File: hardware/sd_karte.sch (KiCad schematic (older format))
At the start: 9 parts, among them CON1 SD_Card

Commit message: Weiter am Schaltplan gezeichnet ... noch sehr Fehlerhaft
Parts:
- renumbered R1 to R2, R2 to R3, R3 to R4, R4 to R5, R5 to R6, R6 to R7
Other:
- moved on the sheet: CON1, D1, D2, R2, R3, R4, R5, R6, R7
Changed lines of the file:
@@
 L SD_Card CON1
 U 1 1 55F7A1C8
-P 6500 3800
-F 0 "CON1" H 5850 4350 50  0000 C CNN
-F 1 "SD_Card" H 7100 3250 50  0000 C CNN
-F 2 "10067847-001" H 6700 4150 50  0000 C CNN
-F 3 "" H 6500 3800 60  0000 C CNN
-	1    6500 3800
+P 6700 3700
+F 0 "CON1" H 6050 4250 50  0000 C CNN
+F 1 "SD_Card" H 7300 3150 50  0000 C CNN
+F 2 "10067847-001" H 6900 4050 50  0000 C CNN
+F 3 "" H 6700 3700 60  0000 C CNN
+	1    6700 3700
 	1    0    0    -1
 $EndComp
 $Comp
-L GND #PWR4
+L GND #PWR010
 U 1 1 55F7A326
-P 5500 4250
-F 0 "#PWR4" H 5500 4000 50  0001 C CNN
-F 1 "GND" H 5500 4100 50  0000 C CNN
-F 2 "" H 5500 4250 60  0000 C CNN
-F 3 "" H 5500 4250 60  0000 C CNN
-	1    5500 4250
+P 5700 4150
+F 0 "#PWR010" H 5700 3900 50  0001 C CNN
+F 1 "GND" H 5700 4000 50  0000 C CNN
+F 2 "" H 5700 4150 60  0000 C CNN
+F 3 "" H 5700 4150 60  0000 C CNN
+	1    5700 4150
 	1    0    0    -1
 $EndComp
@@
 L D D1
 U 1 1 55F7A3CC
-P 5250 4400
-F 0 "D1" H 5250 4500 50  0000 C CNN
-F 1 "1N4148" H 5250 4300 50  0000 C CNN
-F 2 "" H 5250 4400 60  0000 C CNN
-F 3 "" H 5250 4400 60  0000 C CNN
-	1    5250 4400
+P 5450 4300
+F 0 "D1" H 5450 4400 50  0000 C CNN
+F 1 "1N4148" H 5450 4200 50  0000 C CNN
+F 2 "" H 5450 4300 60  0000 C CNN
+F 3 "" H 5450 4300 60  0000 C CNN
+	1    5450 4300
 	0    1    1    0
 $EndComp
@@
 L D D2
 U 1 1 55F7A4EB
-P 5250 4800
-F 0 "D2" H 5250 4900 50  0000 C CNN
-F 1 "1N4148" H 5250 4700 50  0000 C CNN
-F 2 "" H 5250 4800 60  0000 C CNN
-F 3 "" H 5250 4800 60  0000 C CNN
-	1    5250 4800
+P 5450 4700
+F 0 "D2" H 5450 4800 50  0000 C CNN
+F 1 "1N4148" H 5450 4600 50  0000 C CNN
+F 2 "" H 5450 4700 60  0000 C CNN
+F 3 "" H 5450 4700 60  0000 C CNN
+	1    5450 4700
 	0    1    1    0
 $EndComp
 $Comp
-L +5V #PWR5
+L +5V #PWR011
 U 1 1 55F7A887
-P 5250 5050
-F 0 "#PWR5" H 5250 4900 50  0001 C CNN
-F 1 "+5V" H 5250 5190 50  0000 C CNN
-F 2 "" H 5250 5050 60  0000 C CNN
-F 3 "" H 5250 5050 60  0000 C CNN
-	1    5250 5050
+P 5450 4950
+F 0 "#PWR011" H 5450 4800 50  0001 C CNN
+F 1 "+5V" H 5450 5090 50  0000 C CNN
+F 2 "" H 5450 4950 60  0000 C CNN
+F 3 "" H 5450 4950 60  0000 C CNN
+	1    5450 4950
 	-1   0    0    1
 $EndComp
-NoConn ~ 5600 4200
-NoConn ~ 7400 3600
-NoConn ~ 7400 3700
-NoConn ~ 7400 3900
-NoConn ~ 7400 4000
-Text HLabel 4300 4100 0    60   Input ~ 0
+NoConn ~ 5800 4100
+NoConn ~ 7600 3500
+NoConn ~ 7600 3600
+NoConn ~ 7600 3800
+NoConn ~ 7600 3900
+Text HLabel 4250 4000 0    60   Input ~ 0
 MISO
-Text HLabel 4300 3900 0    60   Input ~ 0
+Text HLabel 4250 3800 0    60   Input ~ 0
 SCK
-Text HLabel 4300 3600 0    60   Input ~ 0
+Text HLabel 4250 3500 0    60   Input ~ 0
 MOSI
-Text HLabel 4300 3500 0    60   Input ~ 0
+Text HLabel 4250 3400 0    60   Input ~ 0
 SS
-NoConn ~ 5600 3400
-$Comp
-L R R4
-U 1 1 55F7B36C
-P 4500 3500
-F 0 "R4" V 4580 3500 50  0000 C CNN
-F 1 "1,8k" V 4500 3500 50  0000 C CNN
-F 2 "" V 4430 3500 30  0000 C CNN
-F 3 "" H 4500 3500 30  0000 C CNN
-	1    4500 3500
-	0    1    1    0
-$EndComp
+NoConn ~ 5800 3300
 $Comp
 L R R5
-U 1 1 55F7B401
-P 4700 3600
-F 0 "R5" V 4780 3600 50  0000 C CNN
-F 1 "1,8k" V 4700 3600 50  0000 C CNN
-F 2 "" V 4630 3600 30  0000 C CNN
-F 3 "" H 4700 3600 30  0000 C CNN
-	1    4700 3600
+U 1 1 55F7B36C
+P 4700 3400
+F 0 "R5" V 4780 3400 50  0000 C CNN
+F 1 "1,8k" V 4700 3400 50  0000 C CNN
+F 2 "" V 4630 3400 30  0000 C CNN
+F 3 "" H 4700 3400 30  0000 C CNN
+	1    4700 3400
 	0    1    1    0
 $EndComp
 $Comp
 L R R6
-U 1 1 55F7B48C
-P 4500 3900
-F 0 "R6" V 4580 3900 50  0000 C CNN
-F 1 "1,8k" V 4500 3900 50  0000 C CNN
-F 2 "" V 4430 3900 30  0000 C CNN
-F 3 "" H 4500 3900 30  0000 C CNN
-	1    4500 3900
+U 1 1 55F7B401
+P 4900 3500
+F 0 "R6" V 4980 3500 50  0000 C CNN
+F 1 "1,8k" V 4900 3500 50  0000 C CNN
+F 2 "" V 4830 3500 30  0000 C CNN
+F 3 "" H 4900 3500 30  0000 C CNN
+	1    4900 3500
 	0    1    1    0
 $EndComp
 $Comp
-L R R1
-U 1 1 55F7BA6C
-P 4700 3250
-F 0 "R1" V 4780 3250 50  0000 C CNN
-F 1 "3,3k" V 4700 3250 50  0000 C CNN
-F 2 "" V 4630 3250 30  0000 C CNN
-F 3 "" H 4700 3250 30  0000 C CNN
-	1    4700 3250
-	1    0    0    -1
+L R R7
+U 1 1 55F7B48C
+P 4700 3800
+F 0 "R7" V 4780 3800 50  0000 C CNN
+F 1 "1,8k" V 4700 3800 50  0000 C CNN
+F 2 "" V 4630 3800 30  0000 C CNN
+F 3 "" H 4700 3800 30  0000 C CNN
+	1    4700 3800
+	0    1    1    0
 $EndComp
 $Comp
 L R R2
-U 1 1 55F7BC20
-P 4900 3250
-F 0 "R2" V 4980 3250 50  0000 C CNN
-F 1 "3,3k" V 4900 3250 50  0000 C CNN
-F 2 "" V 4830 3250 30  0000 C CNN
-F 3 "" H 4900 3250 30  0000 C CNN
-	1    4900 3250
+U 1 1 55F7BA6C
+P 4900 3150
+F 0 "R2" V 4980 3150 50  0000 C CNN
+F 1 "3,3k" V 4900 3150 50  0000 C CNN
+F 2 "" V 4830 3150 30  0000 C CNN
+F 3 "" H 4900 3150 30  0000 C CNN
+	1    4900 3150
 	1    0    0    -1
 $EndComp
 $Comp
 L R R3
-U 1 1 55F7BCCD
-P 5100 3250
-F 0 "R3" V 5180 3250 50  0000 C CNN
-F 1 "3,3k" V 5100 3250 50  0000 C CNN
-F 2 "" V 5030 3250 30  0000 C CNN
-F 3 "" H 5100 3250 30  0000 C CNN
-	1    5100 3250
+U 1 1 55F7BC20
+P 5100 3150
+F 0 "R3" V 5180 3150 50  0000 C CNN
+F 1 "3,3k" V 5100 3150 50  0000 C CNN
+F 2 "" V 5030 3150 30  0000 C CNN
+F 3 "" H 5100 3150 30  0000 C CNN
+	1    5100 3150
 	1    0    0    -1
 $EndComp
 $Comp
-L GND #PWR3
+L R R4
+U 1 1 55F7BCCD
+P 5300 3150
+F 0 "R4" V 5380 3150 50  0000 C CNN
+F 1 "3,3k" V 5300 3150 50  0000 C CNN
+F 2 "" V 5230 3150 30  0000 C CNN
+F 3 "" H 5300 3150 30  0000 C CNN
+	1    5300 3150
+	1    0    0    -1
+$EndComp
+$Comp
+L GND #PWR012
 U 1 1 55F7BE30
-P 4900 2850
-F 0 "#PWR3" H 4900 2600 50  0001 C CNN
-F 1 "GND" H 4900 2700 50  0000 C CNN
-F 2 "" H 4900 2850 60  0000 C CNN
-F 3 "" H 4900 2850 60  0000 C CNN
-	1    4900 2850
+P 5100 2750
+F 0 "#PWR012" H 5100 2500 50  0001 C CNN
+F 1 "GND" H 5100 2600 50  0000 C CNN
+F 2 "" H 5100 2750 60  0000 C CNN
+F 3 "" H 5100 2750 60  0000 C CNN
+	1    5100 2750
 	-1   0    0    1
 $EndComp
 Wire Wire Line
-	5250 4650 5250 4550
+	5450 4550 5450 4450
 Wire Wire Line
-	5600 3800 5250 3800
+	5800 3700 5450 3700
 Wire Wire Line
-	5250 3800 5250 4250
+	5450 3700 5450 4150
 Wire Wire Line
-	5250 4950 5250 5050
+	5450 4850 5450 4950
 Wire Wire Line
-	5600 4100 4300 4100
+	5800 4000 4250 4000
 Wire Wire Line
-	4300 3500 4350 3500
+	4250 3400 4550 3400
 Wire Wire Line
-	4650 3500 5600 3500
+	4850 3400 5800 3400
 Wire Wire Line
-	4850 3600 5600 3600
+	5050 3500 5800 3500
 Wire Wire Line
-	4550 3600 4300 3600
+	4750 3500 4250 3500
 Wire Wire Line
-	4300 3900 4350 3900
+	4250 3800 4550 3800
 Wire Wire Line
-	4650 3900 5600 3900
+	4850 3800 5800 3800
 Wire Wire Line
-	4700 3400 4700 3500
-Connection ~ 4700 3500
+	4900 3300 4900 3400
+Connection ~ 4900 3400
 Wire Wire Line
-	4900 3400 4900 3600
-Connection ~ 4900 3600
+	5100 3300 5100 3500
+Connection ~ 5100 3500
 Wire Wire Line
-	5100 3400 5100 3900
-Connection ~ 5100 3900
+	5300 3300 5300 3800
+Connection ~ 5300 3800
 Wire Wire Line
-	4900 2850 4900 3100
+	5100 2750 5100 3000
 Wire Wire Line
-	5100 2950 5100 3100
+	5300 2850 5300 3000
 Wire Wire Line
-	4700 2950 5100 2950
-Connection ~ 4900 2950
+	4900 2850 5300 2850
+Connection ~ 5100 2850
 Wire Wire Line
-	4700 3100 4700 2950
+	4900 3000 4900 2850
 Wire Wire Line
-	5600 3700 5500 3700
+	5800 3600 5700 3600
 Wire Wire Line
-	5500 3700 5500 4250
+	5700 3600 5700 4150
 Wire Wire Line
-	5600 4000 5500 4000
-Connection ~ 5500 4000
+	5800 3900 5700 3900
+Connection ~ 5700 3900
 $EndSCHEMATC

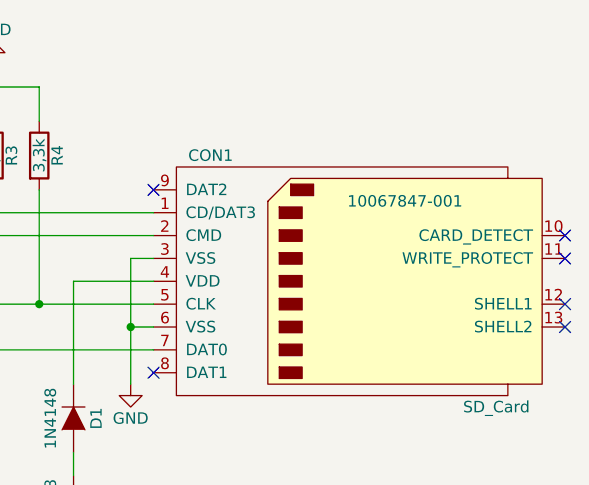
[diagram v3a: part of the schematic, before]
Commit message: Schaltplan weiter entwickelt und Layout angefangen
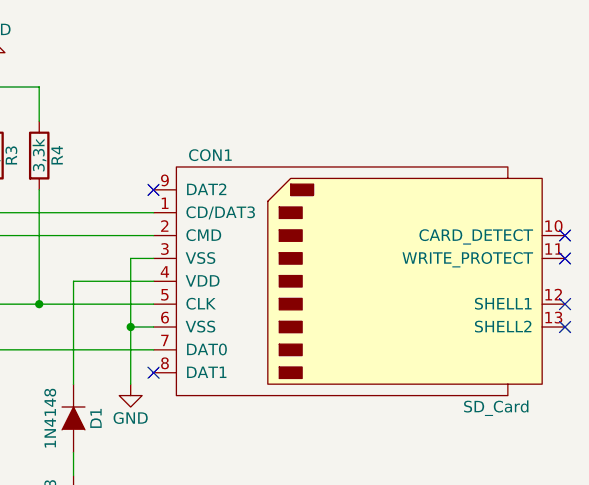
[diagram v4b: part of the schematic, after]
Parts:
- CON1: footprint 10067847-001 -> Connect:SD_Card_Receptacle
- D1, D2: footprint (none) -> Diodes_ThroughHole:Diode_DO-35_SOD27_Horizontal_RM10
- R2, R3, R4, R5, R6, R7: footprint (none) -> Resistors_ThroughHole:Resistor_Horizontal_RM10mm
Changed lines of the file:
@@
 $Descr A4 11693 8268
 encoding utf-8
-Sheet 2 2
+Sheet 2 4
 Title "1541-rebuid"
 Date "2015-09-15"
@@
 F 0 "CON1" H 6050 4250 50  0000 C CNN
 F 1 "SD_Card" H 7300 3150 50  0000 C CNN
-F 2 "10067847-001" H 6900 4050 50  0000 C CNN
+F 2 "Connect:SD_Card_Receptacle" H 6900 4050 50  0001 C CNN
 F 3 "" H 6700 3700 60  0000 C CNN
 	1    6700 3700
@@
 $EndComp
 $Comp
-L GND #PWR010
+L GND #PWR08
 U 1 1 55F7A326
 P 5700 4150
-F 0 "#PWR010" H 5700 3900 50  0001 C CNN
+F 0 "#PWR08" H 5700 3900 50  0001 C CNN
 F 1 "GND" H 5700 4000 50  0000 C CNN
 F 2 "" H 5700 4150 60  0000 C CNN
@@
 F 0 "D1" H 5450 4400 50  0000 C CNN
 F 1 "1N4148" H 5450 4200 50  0000 C CNN
-F 2 "" H 5450 4300 60  0000 C CNN
+F 2 "Diodes_ThroughHole:Diode_DO-35_SOD27_Horizontal_RM10" H 5450 4300 60  0001 C CNN
 F 3 "" H 5450 4300 60  0000 C CNN
 	1    5450 4300
@@
 F 0 "D2" H 5450 4800 50  0000 C CNN
 F 1 "1N4148" H 5450 4600 50  0000 C CNN
-F 2 "" H 5450 4700 60  0000 C CNN
+F 2 "Diodes_ThroughHole:Diode_DO-35_SOD27_Horizontal_RM10" H 5450 4700 60  0001 C CNN
 F 3 "" H 5450 4700 60  0000 C CNN
 	1    5450 4700
@@
 $EndComp
 $Comp
-L +5V #PWR011
+L +5V #PWR09
 U 1 1 55F7A887
 P 5450 4950
-F 0 "#PWR011" H 5450 4800 50  0001 C CNN
+F 0 "#PWR09" H 5450 4800 50  0001 C CNN
 F 1 "+5V" H 5450 5090 50  0000 C CNN
 F 2 "" H 5450 4950 60  0000 C CNN
@@
 F 0 "R5" V 4780 3400 50  0000 C CNN
 F 1 "1,8k" V 4700 3400 50  0000 C CNN
-F 2 "" V 4630 3400 30  0000 C CNN
+F 2 "Resistors_ThroughHole:Resistor_Horizontal_RM10mm" V 4630 3400 30  0001 C CNN
 F 3 "" H 4700 3400 30  0000 C CNN
 	1    4700 3400
@@
 F 0 "R6" V 4980 3500 50  0000 C CNN
 F 1 "1,8k" V 4900 3500 50  0000 C CNN
-F 2 "" V 4830 3500 30  0000 C CNN
+F 2 "Resistors_ThroughHole:Resistor_Horizontal_RM10mm" V 4830 3500 30  0001 C CNN
 F 3 "" H 4900 3500 30  0000 C CNN
 	1    4900 3500
@@
 F 0 "R7" V 4780 3800 50  0000 C CNN
 F 1 "1,8k" V 4700 3800 50  0000 C CNN
-F 2 "" V 4630 3800 30  0000 C CNN
+F 2 "Resistors_ThroughHole:Resistor_Horizontal_RM10mm" V 4630 3800 30  0001 C CNN
 F 3 "" H 4700 3800 30  0000 C CNN
 	1    4700 3800
@@
 F 0 "R2" V 4980 3150 50  0000 C CNN
 F 1 "3,3k" V 4900 3150 50  0000 C CNN
-F 2 "" V 4830 3150 30  0000 C CNN
+F 2 "Resistors_ThroughHole:Resistor_Horizontal_RM10mm" V 4830 3150 30  0001 C CNN
 F 3 "" H 4900 3150 30  0000 C CNN
 	1    4900 3150
@@
 F 0 "R3" V 5180 3150 50  0000 C CNN
 F 1 "3,3k" V 5100 3150 50  0000 C CNN
-F 2 "" V 5030 3150 30  0000 C CNN
+F 2 "Resistors_ThroughHole:Resistor_Horizontal_RM10mm" V 5030 3150 30  0001 C CNN
 F 3 "" H 5100 3150 30  0000 C CNN
 	1    5100 3150
@@
 F 0 "R4" V 5380 3150 50  0000 C CNN
 F 1 "3,3k" V 5300 3150 50  0000 C CNN
-F 2 "" V 5230 3150 30  0000 C CNN
+F 2 "Resistors_ThroughHole:Resistor_Horizontal_RM10mm" V 5230 3150 30  0001 C CNN
 F 3 "" H 5300 3150 30  0000 C CNN
 	1    5300 3150
@@
 $EndComp
 $Comp
-L GND #PWR012
+L GND #PWR010
 U 1 1 55F7BE30
 P 5100 2750
-F 0 "#PWR012" H 5100 2500 50  0001 C CNN
+F 0 "#PWR010" H 5100 2500 50  0001 C CNN
 F 1 "GND" H 5100 2600 50  0000 C CNN
 F 2 "" H 5100 2750 60  0000 C CNN

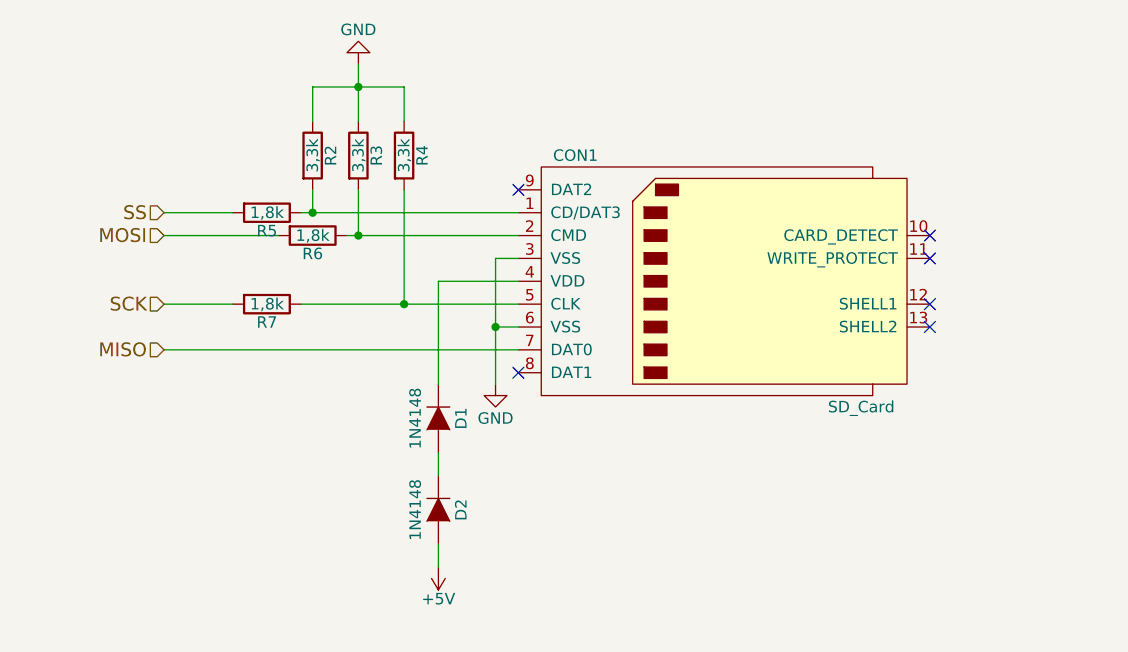
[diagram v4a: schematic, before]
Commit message: Sourcecode neu überarbeitet, Schaltplan angepasst und DOC bearbeitet
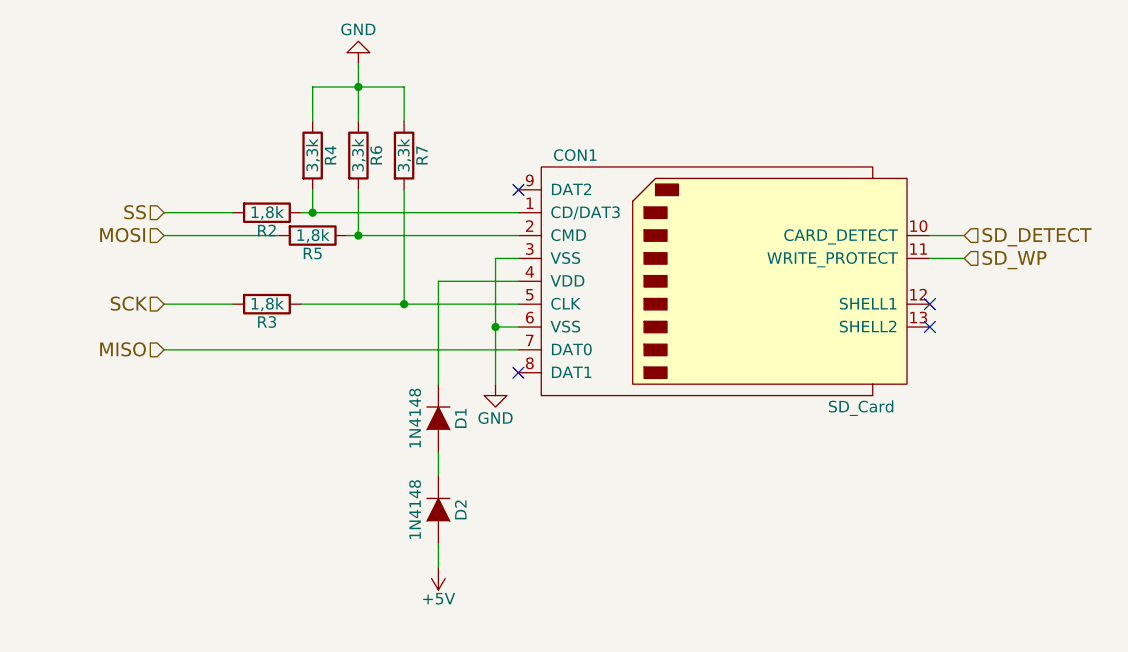
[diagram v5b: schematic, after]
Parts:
- renumbered R5 to R2, R7 to R3, R2 to R4, R6 to R5, R3 to R6, R4 to R7
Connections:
- net SD_DETECT: now reaches CON1.10 (CARD_DETECT)
- net SD_WP: now reaches CON1.11 (WRITE_PROTECT)
- no-connect marks 6 -> 4
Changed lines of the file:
@@
 $EndComp
 NoConn ~ 5800 4100
-NoConn ~ 7600 3500
-NoConn ~ 7600 3600
 NoConn ~ 7600 3800
 NoConn ~ 7600 3900
@@
 NoConn ~ 5800 3300
 $Comp
-L R R5
+L R R2
 U 1 1 55F7B36C
 P 4700 3400
-F 0 "R5" V 4780 3400 50  0000 C CNN
+F 0 "R2" V 4780 3400 50  0000 C CNN
 F 1 "1,8k" V 4700 3400 50  0000 C CNN
 F 2 "Resistors_ThroughHole:Resistor_Horizontal_RM10mm" V 4630 3400 30  0001 C CNN
@@
 $EndComp
 $Comp
-L R R6
+L R R5
 U 1 1 55F7B401
 P 4900 3500
-F 0 "R6" V 4980 3500 50  0000 C CNN
+F 0 "R5" V 4980 3500 50  0000 C CNN
 F 1 "1,8k" V 4900 3500 50  0000 C CNN
 F 2 "Resistors_ThroughHole:Resistor_Horizontal_RM10mm" V 4830 3500 30  0001 C CNN
@@
 $EndComp
 $Comp
-L R R7
+L R R3
 U 1 1 55F7B48C
 P 4700 3800
-F 0 "R7" V 4780 3800 50  0000 C CNN
+F 0 "R3" V 4780 3800 50  0000 C CNN
 F 1 "1,8k" V 4700 3800 50  0000 C CNN
 F 2 "Resistors_ThroughHole:Resistor_Horizontal_RM10mm" V 4630 3800 30  0001 C CNN
@@
 $EndComp
 $Comp
-L R R2
+L R R4
 U 1 1 55F7BA6C
 P 4900 3150
-F 0 "R2" V 4980 3150 50  0000 C CNN
+F 0 "R4" V 4980 3150 50  0000 C CNN
 F 1 "3,3k" V 4900 3150 50  0000 C CNN
 F 2 "Resistors_ThroughHole:Resistor_Horizontal_RM10mm" V 4830 3150 30  0001 C CNN
@@
 $EndComp
 $Comp
-L R R3
+L R R6
 U 1 1 55F7BC20
 P 5100 3150
-F 0 "R3" V 5180 3150 50  0000 C CNN
+F 0 "R6" V 5180 3150 50  0000 C CNN
 F 1 "3,3k" V 5100 3150 50  0000 C CNN
 F 2 "Resistors_ThroughHole:Resistor_Horizontal_RM10mm" V 5030 3150 30  0001 C CNN
@@
 $EndComp
 $Comp
-L R R4
+L R R7
 U 1 1 55F7BCCD
 P 5300 3150
-F 0 "R4" V 5380 3150 50  0000 C CNN
+F 0 "R7" V 5380 3150 50  0000 C CNN
 F 1 "3,3k" V 5300 3150 50  0000 C CNN
 F 2 "Resistors_ThroughHole:Resistor_Horizontal_RM10mm" V 5230 3150 30  0001 C CNN
@@
 	5800 3900 5700 3900
 Connection ~ 5700 3900
+Text HLabel 7750 3500 2    60   Input ~ 0
+SD_DETECT
+Text HLabel 7750 3600 2    60   Input ~ 0
+SD_WP
+Wire Wire Line
+	7750 3500 7600 3500
+Wire Wire Line
+	7750 3600 7600 3600
 $EndSCHEMATC

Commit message: diverese Sachen geändert
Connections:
- net SD_DETECT: no longer names the net of CON1.10 (CARD_DETECT)
- net SD_WP: no longer names the net of CON1.11 (WRITE_PROTECT)
- no-connect marks 4 -> 6
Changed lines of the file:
@@
 $EndComp
 $Comp
-L GND #PWR09
+L GND #PWR011
 U 1 1 55F7A326
 P 5700 4150
-F 0 "#PWR09" H 5700 3900 50  0001 C CNN
+F 0 "#PWR011" H 5700 3900 50  0001 C CNN
 F 1 "GND" H 5700 4000 50  0000 C CNN
 F 2 "" H 5700 4150 60  0000 C CNN
@@
 $EndComp
 $Comp
-L +5V #PWR010
+L +5V #PWR012
 U 1 1 55F7A887
 P 5450 4950
-F 0 "#PWR010" H 5450 4800 50  0001 C CNN
+F 0 "#PWR012" H 5450 4800 50  0001 C CNN
 F 1 "+5V" H 5450 5090 50  0000 C CNN
 F 2 "" H 5450 4950 60  0000 C CNN
@@
 $EndComp
 $Comp
-L GND #PWR011
+L GND #PWR013
 U 1 1 55F7BE30
 P 5100 2750
-F 0 "#PWR011" H 5100 2500 50  0001 C CNN
+F 0 "#PWR013" H 5100 2500 50  0001 C CNN
 F 1 "GND" H 5100 2600 50  0000 C CNN
 F 2 "" H 5100 2750 60  0000 C CNN
@@
 	5800 3900 5700 3900
 Connection ~ 5700 3900
-Text HLabel 7750 3500 2    60   Input ~ 0
+Text HLabel 4250 4300 0    60   Input ~ 0
 SD_DETECT
-Text HLabel 7750 3600 2    60   Input ~ 0
+Text HLabel 4250 4450 0    60   Input ~ 0
 SD_WP
-Wire Wire Line
-	7750 3500 7600 3500
-Wire Wire Line
-	7750 3600 7600 3600
+$Comp
+L GND #PWR014
+U 1 1 583A74DE
+P 4450 4550
+F 0 "#PWR014" H 4450 4300 50  0001 C CNN
+F 1 "GND" H 4450 4400 50  0000 C CNN
+F 2 "" H 4450 4550 60  0000 C CNN
+F 3 "" H 4450 4550 60  0000 C CNN
+	1    4450 4550
+	1    0    0    -1
+$EndComp
+Wire Wire Line
+	4450 4550 4450 4300
+Wire Wire Line
+	4450 4300 4250 4300
+Wire Wire Line
+	4250 4450 4450 4450
+Connection ~ 4450 4450
+NoConn ~ 7600 3500
+NoConn ~ 7600 3600
 $EndSCHEMATC
